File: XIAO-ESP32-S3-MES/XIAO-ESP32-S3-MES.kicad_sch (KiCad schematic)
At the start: 12 parts, among them J1 Conn_01x04_Socket, J2 Conn_01x03_Socket, J3 Conn_01x04_Socket, J6 Conn_01x02_Pin, U2 XIAO-ESP32-S3-SMD

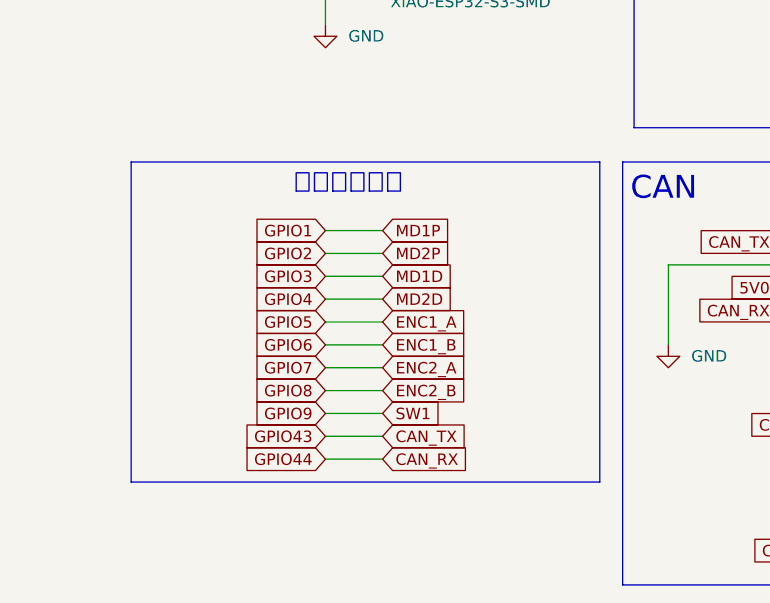
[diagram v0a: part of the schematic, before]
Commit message: MES 回路図完成
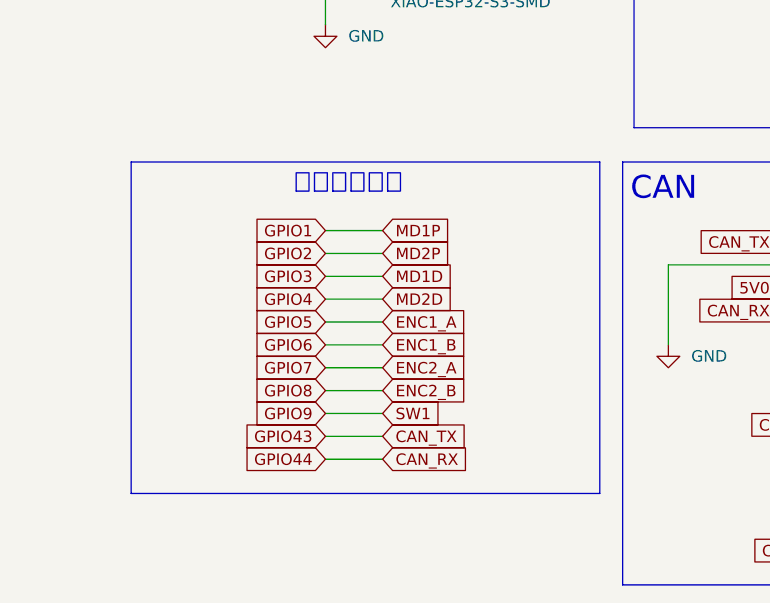
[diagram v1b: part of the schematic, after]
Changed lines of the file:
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@@
 	(rectangle
 		(start 27.94 97.79)
-		(end 80.01 133.35)
+		(end 80.01 134.62)
 		(stroke
 			(width 0)

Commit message: 一旦配置
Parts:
- removed J2: Conn_01x03_Socket, Connector_JST:JST_XH_B3B-XH-A_1x03_P2.50mm_Vertical, symbol Connector:Conn_01x03_Socket
- removed J6: Conn_01x02_Pin, Connector_AMASS:AMASS_XT30U-M_1x02_P5.0mm_Vertical, symbol Connector:Conn_01x02_Pin
- added J2: Conn_01x02_Socket, Connector_JST:JST_XH_B2B-XH-A_1x02_P2.50mm_Vertical, symbol Connector:Conn_01x02_Socket
- renumbered R3 to R1
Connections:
- net GND: now also J2.2 (Pin_2)
- net GPIO9: now also J2.1 (Pin_1)

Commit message: 汎用性重視
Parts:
- added MD3: MD3, Connector_JST:JST_XH_B4B-XH-A_1x04_P2.50mm_Vertical, symbol Connector:Conn_01x04_Pin
- added MD4: MD4, Connector_JST:JST_XH_B4B-XH-A_1x04_P2.50mm_Vertical, symbol Connector:Conn_01x04_Pin
- added SW2: SW2, Connector_JST:JST_XH_B2B-XH-A_1x02_P2.50mm_Vertical, symbol Connector:Conn_01x02_Socket
- added SW3: SW3, Connector_JST:JST_XH_B2B-XH-A_1x02_P2.50mm_Vertical, symbol Connector:Conn_01x02_Socket
- added SW4: SW4, Connector_JST:JST_XH_B2B-XH-A_1x02_P2.50mm_Vertical, symbol Connector:Conn_01x02_Socket
- added SW5: SW5, Connector_JST:JST_XH_B2B-XH-A_1x02_P2.50mm_Vertical, symbol Connector:Conn_01x02_Socket
- SW1: renamed from J2; value Conn_01x02_Socket -> SW1
- renumbered J3 to J2
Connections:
- net 5V0: now also MD3.1 (Pin_1), MD4.1 (Pin_1)
- net ENC1_A: now also MD3.3 (Pin_3), SW2.1 (Pin_1)
- net ENC1_B: now also MD3.4 (Pin_4), SW3.1 (Pin_1)
- net ENC2_A: now also MD4.3 (Pin_3), SW4.1 (Pin_1)
- net ENC2_B: now also MD4.4 (Pin_4), SW5.1 (Pin_1)
- net GND: now also MD3.2 (Pin_2), MD4.2 (Pin_2), SW2.2 (Pin_2), SW3.2 (Pin_2), SW4.2 (Pin_2), SW5.2 (Pin_2)
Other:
- moved on the sheet: J1, J2, MD1, MD2, R1, R120, SW1, U1

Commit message: MES配置完了
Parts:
- removed MD3: MD3, Connector_JST:JST_XH_B4B-XH-A_1x04_P2.50mm_Vertical, symbol Connector:Conn_01x04_Pin
- removed MD4: MD4, Connector_JST:JST_XH_B4B-XH-A_1x04_P2.50mm_Vertical, symbol Connector:Conn_01x04_Pin
- removed SW4: SW4, Connector_JST:JST_XH_B2B-XH-A_1x02_P2.50mm_Vertical, symbol Connector:Conn_01x02_Socket
- removed SW5: SW5, Connector_JST:JST_XH_B2B-XH-A_1x02_P2.50mm_Vertical, symbol Connector:Conn_01x02_Socket
- renumbered J1 to CAN1, J2 to CAN2
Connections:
- net ENC1_A: no longer SW2.1 (Pin_1)
- net ENC1_B: no longer SW3.1 (Pin_1)
- net ENC2_A renamed ENC2_A/SW2
- net ENC2_A/SW2: now also SW2.1 (Pin_1)
- net ENC2_B renamed ENC2_B/SW3
- net ENC2_B/SW3: now also SW3.1 (Pin_1)
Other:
- note added: "スイッチ"
- note removed: "デジタル入力"
- moved on the sheet: ENC1, ENC2, SW1
